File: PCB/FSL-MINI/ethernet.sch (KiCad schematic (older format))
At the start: 43 parts, among them P201 SI-52003-F, P202 PoE, U201 LAN8720A-CP, U202 SI502

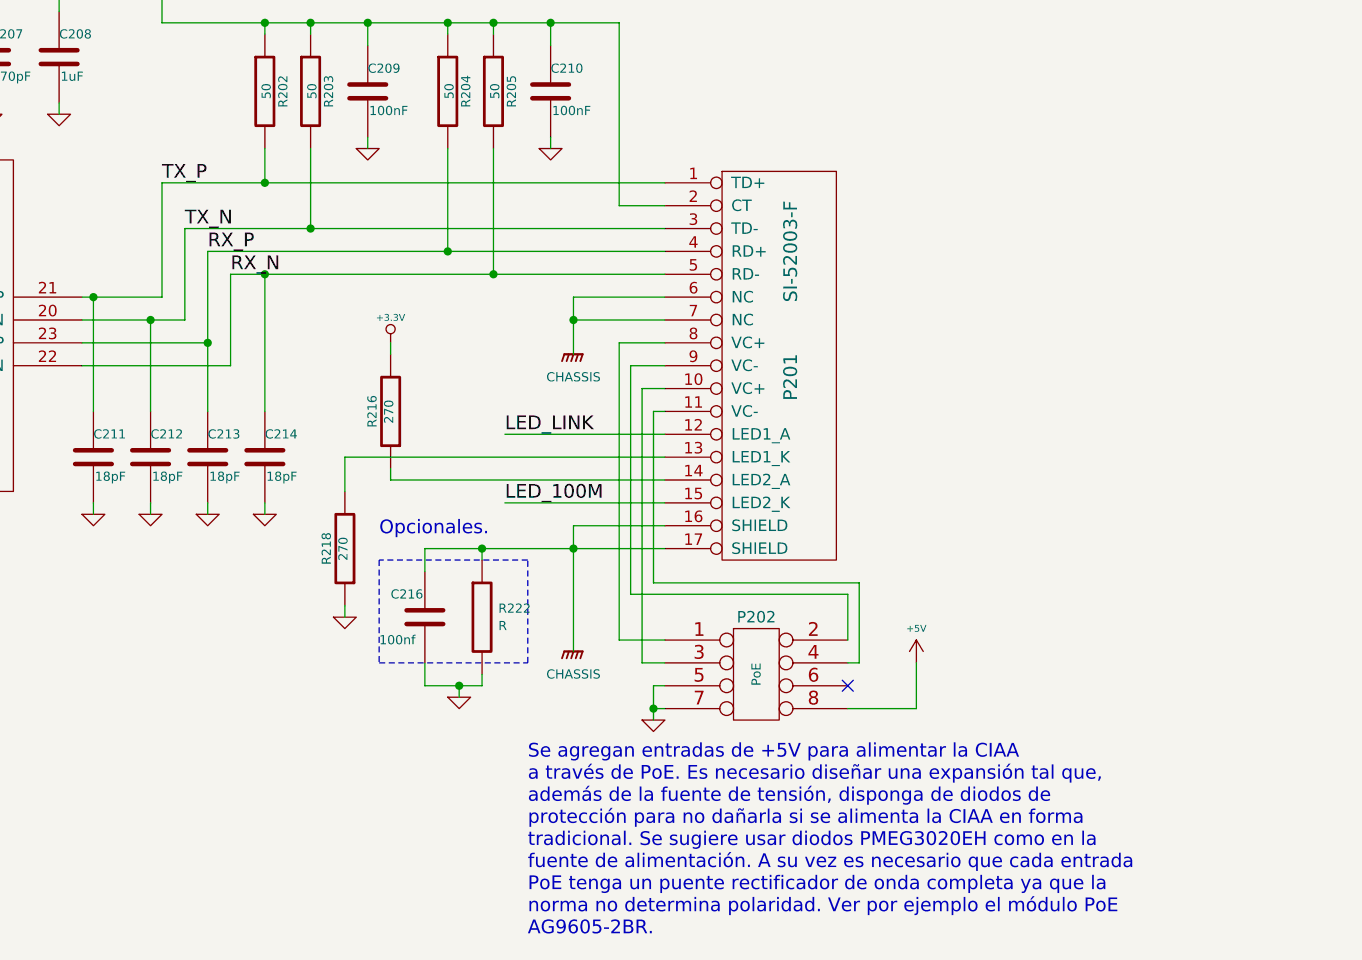
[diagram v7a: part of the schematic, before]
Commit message: Modificación en esquemático del conector JTAG. Eliminación en esquemático y pcb del conector PoE.
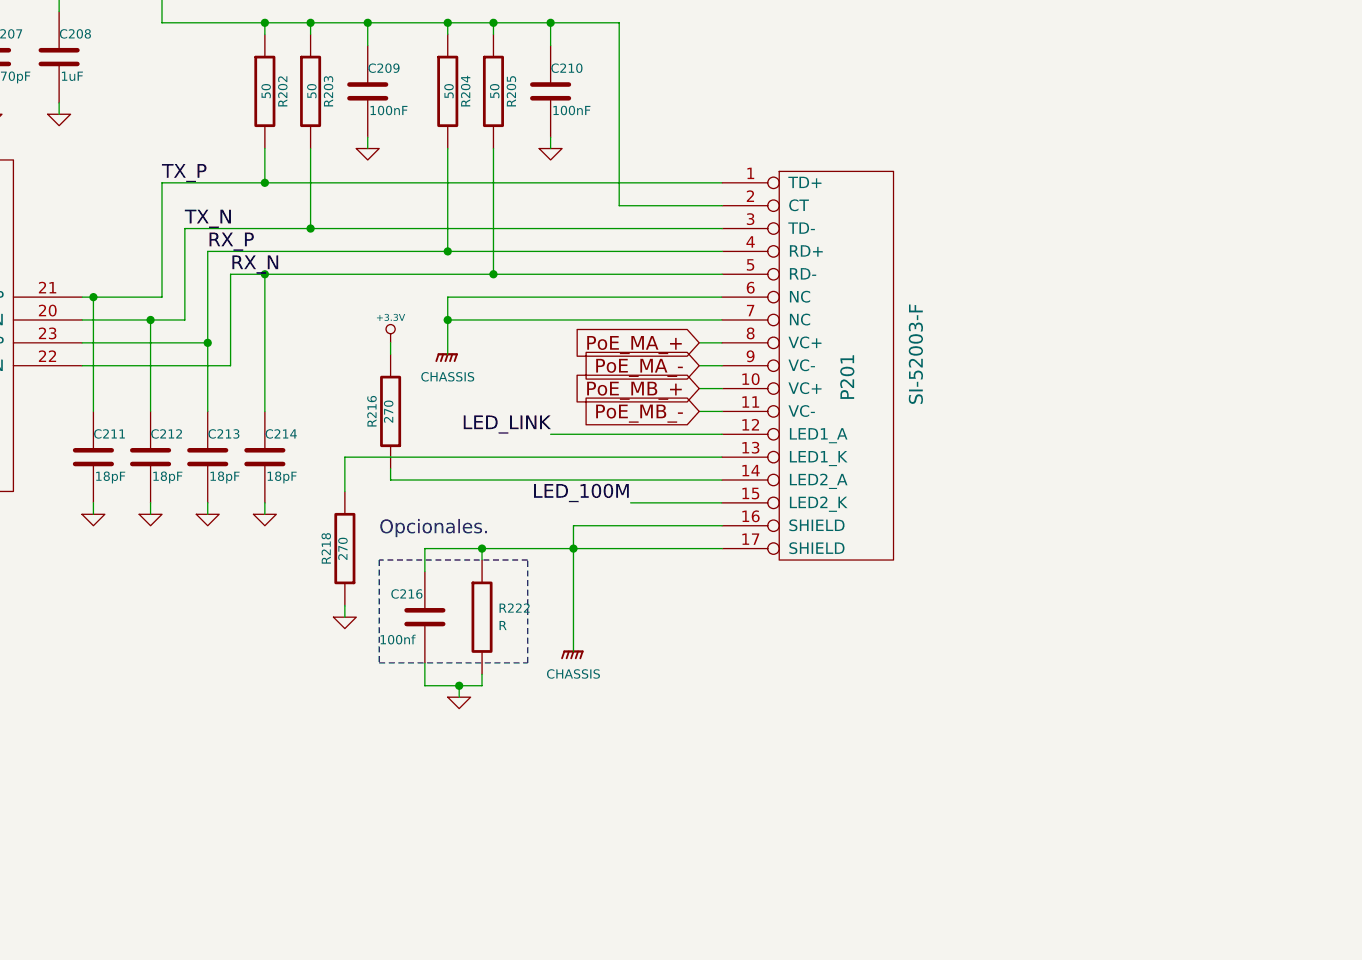
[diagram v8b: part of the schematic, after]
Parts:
- removed P202: PoE, Pin_Headers:Pin_Header_Straight_2x04, symbol CONN_4X2
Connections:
- net PoE_MA_+: now reaches P201.8 (VC+)
- net PoE_MA_-: now reaches P201.9 (VC-)
- net PoE_MB_+: now reaches P201.10 (VC+)
- net PoE_MB_-: now reaches P201.11 (VC-)
- no-connect marks 2 -> 1
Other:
- note removed: "Se agregan entradas de +5V para alimentar la CIAA\na través de PoE. Es necesario diseñar una expansión tal que, \nademás de la fuente de tensión, disponga de diodos de \nprotección para no dañarla si se alimenta la CIAA en forma \ntradicional. Se sugiere usar diodos PMEG3020EH como en la \nfuente de alimentación. A su vez es necesario que cada entrada\nPoE tenga un puente rectificador de onda com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"
- moved on the sheet: P201
